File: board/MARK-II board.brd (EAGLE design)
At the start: 130 x 80 mm, 169 parts, among them IC1 MAX3243CPWR, IC10 IFX1963TBV, IC11 IFX1963TBV, IC12 ATMEGA48PB-AU, IC13 LD1117S33, IC2 FT230XS, IC3 ENC28J60SS, IC4 PCM5100, IC5 IS42S83200, IC6 MCP7940NSN, IC7 FM24CL16BG, IC8 AT25DN256SS, IC9 10M25SAE144, Q1 25MHz, Q2 32.768kHz, Q3 CMI-1275C-050, Q4 25MHz, Q5 18,432MHz, Q6 22.5792MHz, T1 BC337-16 A1, X1 MINI-USBUX60A-MB-5ST, X10 T821-106A1S100, X11 T821-110A1S100, X12 PJ-002BH-SMT-TR, X13 T821-106A1S100, X2 L717SDE09P1ACH4F, X3 L77HDE15SD1CH4R, X4 MD-60SM, X5 RB1-125BAG1A, X6 SJ1-3535NG, X7 MICROSD-HRS_DM3D, X8 BAT-HLD-002-SMT, X9 T821-120A1S100

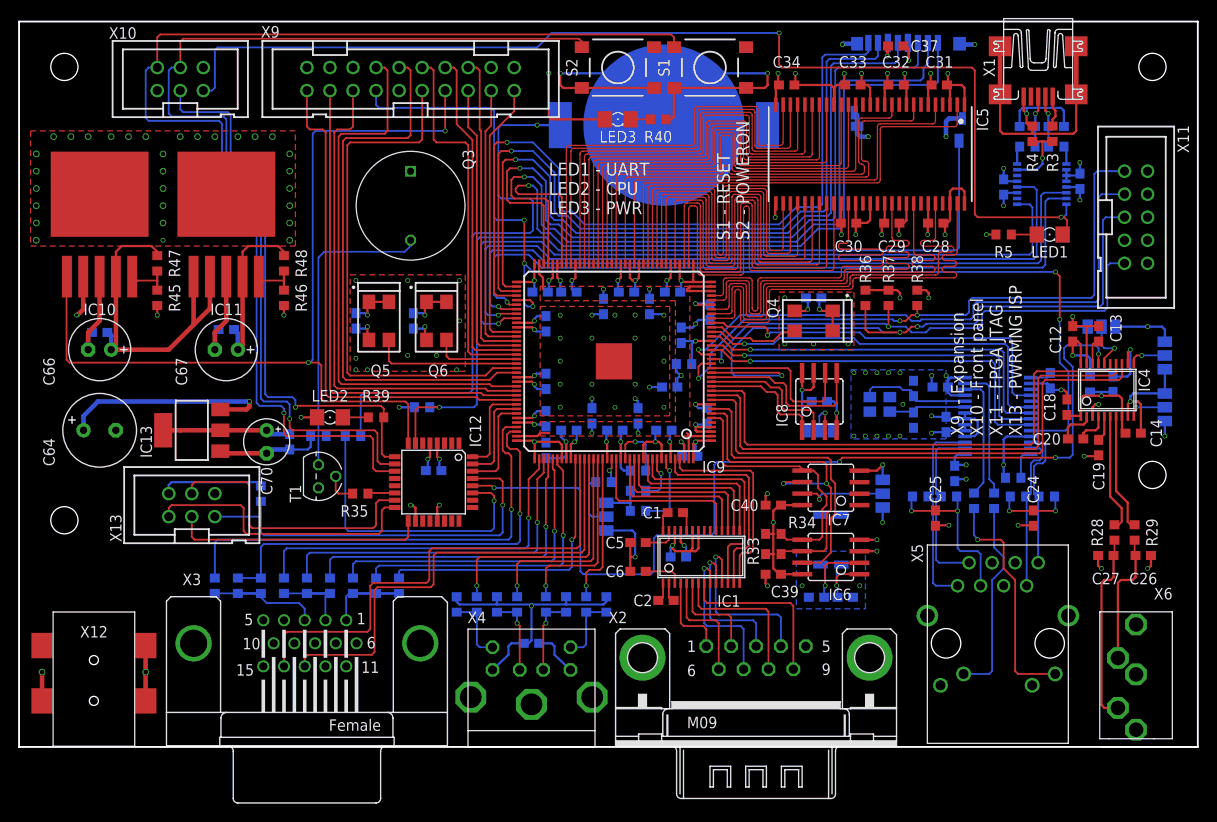
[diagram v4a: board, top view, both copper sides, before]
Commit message: Fixed some mistakes on board design
Enc xtal is now on top side
Changed barrel jack holes diameter
Fixed pins pitch on mini DIN con
Changed value of input capacitor
Fixed position of RS232 Dsub con, changed part number
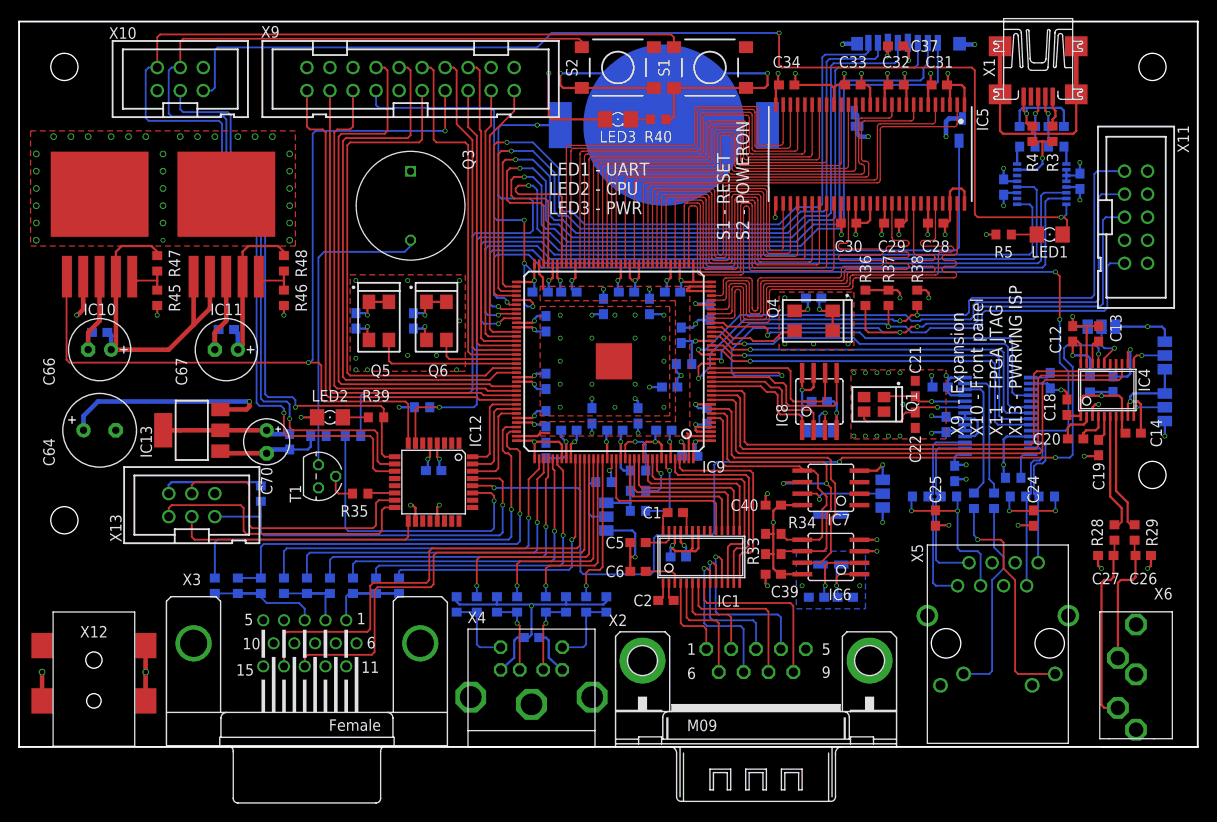
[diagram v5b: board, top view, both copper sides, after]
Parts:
- C64: value 1000u -> 470u
- X2: value L717SDE09P1ACH4F -> 5504F1-09P-02A-03
- moved Q1 0.64 mm to (94.3, 37.8), flipped to the top
- moved C10 0.63 mm to (56.5, 12.1)
- moved X2 0.32 mm to (81.3, 9.53)
- moved C21 0.20 mm to (98.8, 39.5), flipped to the top
- moved C22 0.20 mm to (98.8, 36.0), flipped to the top
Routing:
- net N$19: track 8.75 -> 13.4 mm, vias 0 -> 1
- net N$18: track 12.4 -> 9.38 mm, vias 0 -> 1
- net N$9: track 7.64 -> 8.54 mm
- net N$33: track 7.64 -> 8.54 mm
- net +5V: track 221.6 -> 220.9 mm

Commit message: Add ferrite beads
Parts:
- FB1, FB2: value (none) -> BLM18AG601SN1D
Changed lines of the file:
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@@
 <attribute name="VALUE" x="72.39" y="37.7825" size="1.27" layer="28" rot="MR0"/>
 </element>
-<element name="FB1" library="misc" package="R0603" value="" x="118.11" y="40.005" smashed="yes" rot="MR270">
+<element name="FB1" library="misc" package="R0603" value="BLM18AG601SN1D" x="118.11" y="40.005" smashed="yes" rot="MR270">
+<attribute name="MOUSER" value="81-BLM11A601S" x="118.11" y="40.005" size="1.778" layer="28" rot="MR270" display="off"/>
 <attribute name="NAME" x="118.11" y="36.83" size="1.27" layer="26" font="vector" rot="MR270" align="center"/>
 <attribute name="VALUE" x="120.015" y="40.64" size="1.27" layer="28" rot="MR270"/>
 </element>
-<element name="FB2" library="misc" package="R0603" value="" x="73.3425" y="42.2275" smashed="yes" rot="MR0">
+<element name="FB2" library="misc" package="R0603" value="BLM18AG601SN1D" x="73.3425" y="42.2275" smashed="yes" rot="MR0">
+<attribute name="MOUSER" value="81-BLM11A601S" x="73.3425" y="42.2275" size="1.778" layer="28" rot="MR0" display="off"/>
 <attribute name="NAME" x="75.8825" y="42.2275" size="1.27" layer="26" font="vector" rot="MR90" align="center"/>
 <attribute name="VALUE" x="73.9775" y="40.3225" size="1.27" layer="28" rot="MR0"/>

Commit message: Fixed some mistakes in component names
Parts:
- IC5: value IS42S83200 -> AS4C32M8SA
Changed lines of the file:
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@@
 <attribute name="VALUE" x="76.61" y="55.435" size="1.27" layer="27" rot="R180"/>
 </element>
-<element name="IC5" library="ic" package="TSOP54" value="IS42S83200" x="93.8675" y="65.39" smashed="yes" rot="R180">
+<element name="IC5" library="ic" package="TSOP54" value="AS4C32M8SA" x="93.8675" y="65.39" smashed="yes" rot="R180">
 <attribute name="MOUSER" value="913-AS4C32M8SA6TIN" x="93.8675" y="65.39" size="1.778" layer="27" rot="R180" display="off"/>
 <attribute name="NAME" x="106.25" y="69.2" size="1.27" layer="25" font="vector" rot="R270" align="center"/>
@@
 </element>
 <element name="C64" library="misc" package="E3,5-8" value="470u" x="8.89" y="34.925" smashed="yes">
-<attribute name="MOUSER" value="667-EEU-FR1C102L" x="8.89" y="34.925" size="1.778" layer="27" display="off"/>
+<attribute name="MOUSER" value="667-EEU-FR1E471Y" x="8.89" y="34.925" size="1.778" layer="27" display="off"/>
 <attribute name="NAME" x="3.302" y="32.512" size="1.27" layer="25" font="vector" rot="R270" align="center"/>
 <attribute name="VALUE" x="6.604" y="31.877" size="1.27" layer="27" ratio="10"/>
